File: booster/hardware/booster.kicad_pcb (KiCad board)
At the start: 2 copper layers, 41.1 x 16 mm, 5 parts, among them J1 12V_booster, J4 Conn_01x03, U1 LM2940IMP-10/NOPB

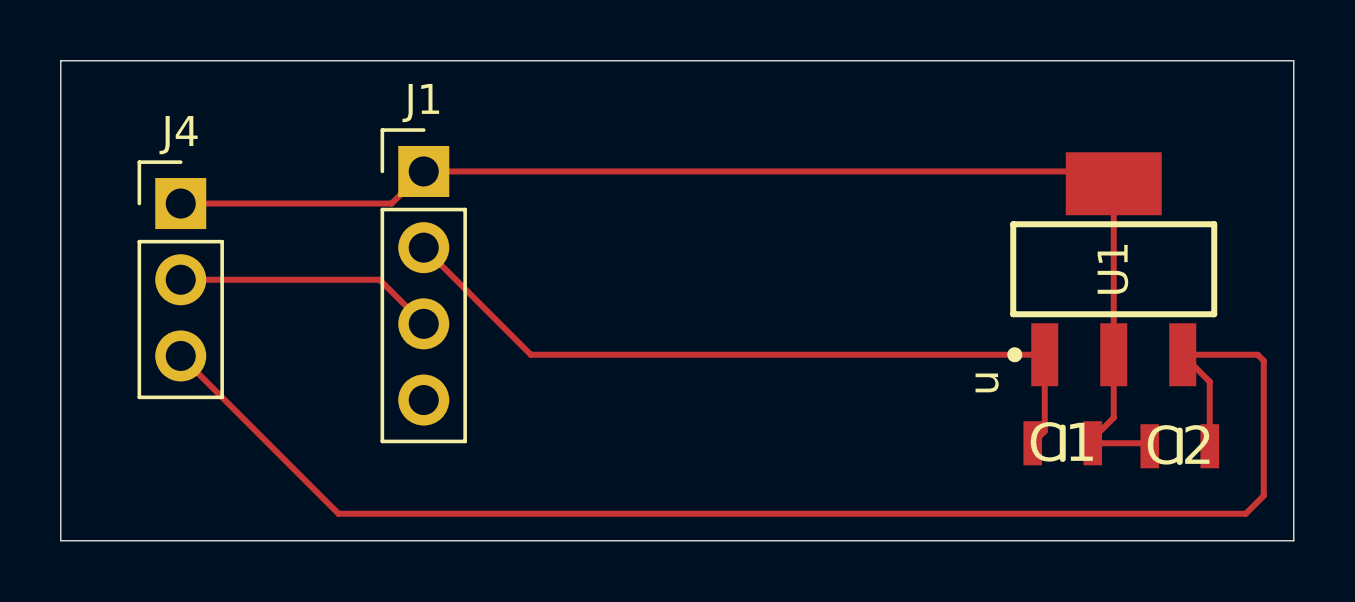
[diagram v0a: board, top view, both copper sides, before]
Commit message: created fab outputs for booster test board
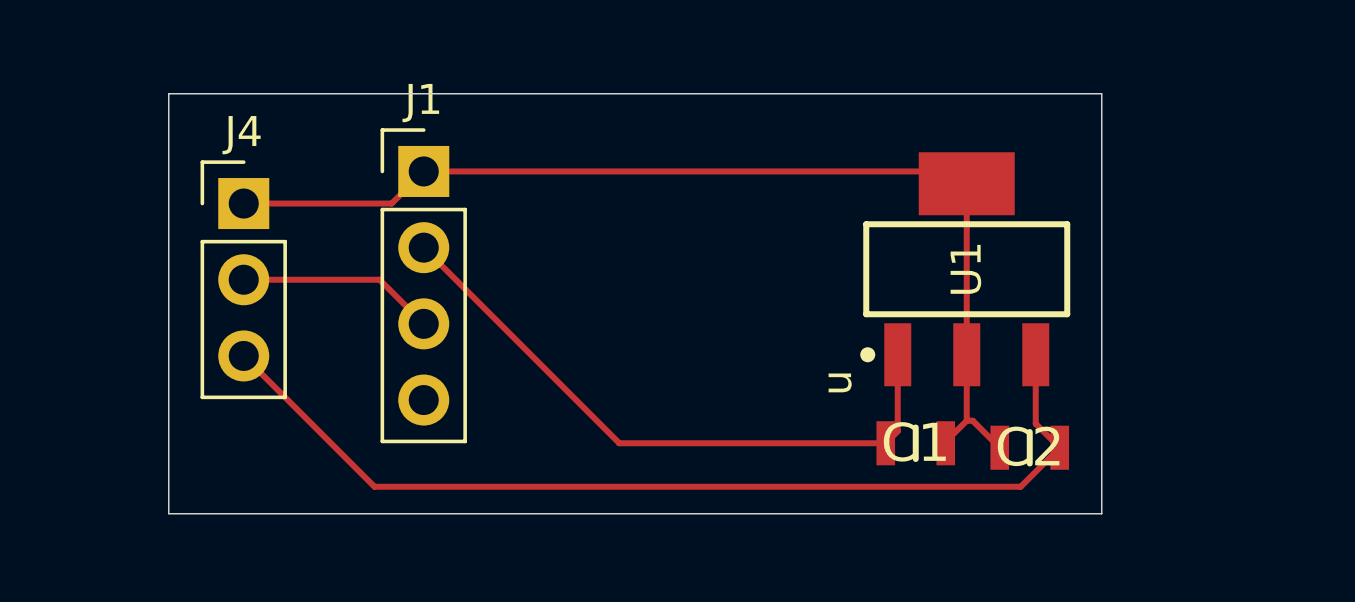
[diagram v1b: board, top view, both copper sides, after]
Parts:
- moved C2 5.00 mm to (147.7, 97.0)
- moved C1 4.90 mm to (143.9, 96.9)
- moved U1 4.90 mm to (145.6, 91.1)
- moved J4 2.10 mm to (121.5, 88.9)
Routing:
- net /10V: track 49.2 -> 33.0 mm
- net GND: track 42.6 -> 35.4 mm
- net /12V: track 25.3 -> 21.2 mm
- net /5V: track 8.71 -> 6.61 mm
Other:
- board size 41.1 x 16 mm -> 31.1 x 14 mm
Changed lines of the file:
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@@
 			(outputformat 1)
 			(mirror no)
-			(drillshape 1)
+			(drillshape 0)
 			(scaleselection 1)
-			(outputdirectory "")
+			(outputdirectory "../outputs/")
 		)
 	)
 	(footprint "Connector_PinHeader_2.54mm:PinHeader_1x03_P2.54mm_Vertical"
 		(layer "F.Cu")
-		(at 119.4 88.86)
+		(at 121.5 88.86)
 		(descr "Through hole straight pin header, 1x03, 2.54mm pitch, single row")
 		(tags "Through hole pin header THT 1x03 2.54mm single row")
@@
 	(footprint "booster:DCY0004A_L"
 		(layer "F.Cu")
-		(at 150.5 91.050001 90)
+		(at 145.6 91.050001 90)
 		(tags "LM2940IMP-10/NOPB ")
 		(property "Reference" "U1"
@@
 	(footprint "booster:CAPC2012X145N"
 		(layer "F.Cu")
-		(at 152.7 96.950001)
+		(at 147.7 97)
 		(descr "C2012 [EIA CC0805]")
 		(tags "Capacitor")
@@
 	(footprint "booster:CAPC2012X145N"
 		(layer "F.Cu")
-		(at 148.8 96.850001 180)
+		(at 143.9 96.850001 180)
 		(descr "C2012 [EIA CC0805]")
 		(tags "Capacitor")
@@
 	)
 	(gr_rect
-		(start 115.4 84.1)
-		(end 156.5 100.1)
+		(start 119 85.2)
+		(end 150.1 99.2)
 		(stroke
 			(width 0.05)
@@
 	)
 	(segment
-		(start 150.089998 87.79)
-		(end 150.5 88.200002)
+		(start 145.6 96.1)
+		(end 145.6 93.9)
 		(width 0.2)
 		(layer "F.Cu")
@@
 	)
 	(segment
-		(start 149.8 96.850001)
-		(end 149.8 96.7)
+		(start 144.9 96.850001)
+		(end 144.9 96.7)
 		(width 0.2)
 		(layer "F.Cu")
@@
 	(segment
 		(start 127.5 87.79)
-		(end 150.089998 87.79)
+		(end 145.189998 87.79)
 		(width 0.2)
 		(layer "F.Cu")
@@
 	)
 	(segment
-		(start 149.8 96.850001)
-		(end 151.6 96.850001)
+		(start 146.7 96.850001)
+		(end 146.8 96.950001)
+		(width 0.2)
+		(layer "F.Cu")
+		(net "GND")
+	)
+	(segment
+		(start 145.189998 87.79)
+		(end 145.6 88.200002)
+		(width 0.2)
+		(layer "F.Cu")
+		(net "GND")
+	)
+	(segment
+		(start 144.9 96.8)
+		(end 145.6 96.1)
+		(width 0.2)
+		(layer "F.Cu")
+		(net "GND")
+	)
+	(segment
+		(start 145.8 96.1)
+		(end 145.6 96.1)
 		(width 0.2)
 		(layer "F.Cu")
@@
 	)
 	(segment
-		(start 151.6 96.850001)
-		(end 151.7 96.950001)
+		(start 146.7 97)
+		(end 145.8 96.1)
 		(width 0.2)
 		(layer "F.Cu")
@@
 	)
 	(segment
-		(start 149.8 96.7)
-		(end 150.5 96)
+		(start 121.5 88.86)
+		(end 126.43 88.86)
 		(width 0.2)
 		(layer "F.Cu")
@@
 	)
 	(segment
-		(start 119.4 88.86)
-		(end 126.43 88.86)
+		(start 144.9 96.850001)
+		(end 144.9 96.8)
 		(width 0.2)
 		(layer "F.Cu")
@@
 	)
 	(segment
-		(start 150.5 88.200002)
-		(end 150.5 93.9)
+		(start 145.6 88.200002)
+		(end 145.6 93.9)
 		(width 0.2)
 		(layer "F.Cu")
 		(net "GND")
-	)
-	(segment
-		(start 150.5 96)
-		(end 150.5 93.9)
-		(width 0.2)
-		(layer "F.Cu")
-		(net "GND")
-	)
-	(segment
-		(start 131.07 93.9)
-		(end 148.2 93.9)
-		(width 0.2)
-		(layer "F.Cu")
-		(net "/12V")
-	)
-	(segment
-		(start 148.2 96.450001)
-		(end 147.8 96.850001)
-		(width 0.2)
-		(layer "F.Cu")
-		(net "/12V")
-	)
-	(segment
-		(start 127.5 90.33)
-		(end 131.07 93.9)
-		(width 0.2)
-		(layer "F.Cu")
-		(net "/12V")
-	)
-	(segment
-		(start 148.2 93.9)
-		(end 148.2 96.450001)
-		(width 0.2)
-		(layer "F.Cu")
-		(net "/12V")
-	)
-	(segment
-		(start 153.7 94.8)
-		(end 152.8 93.9)
-		(width 0.2)
-		(layer "F.Cu")
-		(net "/10V")
-	)
-	(segment
-		(start 155.5 98.6)
-		(end 154.9 99.2)
-		(width 0.2)
-		(layer "F.Cu")
-		(net "/10V")
-	)
-	(segment
-		(start 155.5 94.1)
-		(end 155.5 98.6)
-		(width 0.2)
-		(layer "F.Cu")
-		(net "/10V")
-	)
-	(segment
-		(start 124.66 99.2)
-		(end 119.4 93.94)
-		(width 0.2)
-		(layer "F.Cu")
-		(net "/10V")
-	)
-	(segment
-		(start 154.9 99.2)
-		(end 124.66 99.2)
-		(width 0.2)
-		(layer "F.Cu")
-		(net "/10V")
-	)
-	(segment
-		(start 153.7 96.950001)
-		(end 153.7 94.8)
-		(width 0.2)
-		(layer "F.Cu")
-		(net "/10V")
-	)
-	(segment
-		(start 155.3 93.9)
-		(end 155.5 94.1)
-		(width 0.2)
-		(layer "F.Cu")
-		(net "/10V")
-	)
-	(segment
-		(start 152.8 93.9)
-		(end 155.3 93.9)
-		(width 0.2)
-		(layer "F.Cu")
-		(net "/10V")
-	)
-	(segment
-		(start 126.03 91.4)
-		(end 119.4 91.4)
-		(width 0.2)
-		(layer "F.Cu")
-		(net "/5V")
 	)
 	(segment
@@
 		(net "/5V")
 	)
+	(segment
+		(start 126.03 91.4)
+		(end 121.5 91.4)
+		(width 0.2)
+		(layer "F.Cu")
+		(net "/5V")
+	)
+	(segment
+		(start 148.7 97)
+		(end 147.4 98.3)
+		(width 0.2)
+		(layer "F.Cu")
+		(net "/10V")
+	)
+	(segment
+		(start 125.86 98.3)
+		(end 121.5 93.94)
+		(width 0.2)
+		(layer "F.Cu")
+		(net "/10V")
+	)
+	(segment
+		(start 147.9 96.2)
+		(end 148.7 97)
+		(width 0.2)
+		(layer "F.Cu")
+		(net "/10V")
+	)
+	(segment
+		(start 147.4 98.3)
+		(end 125.86 98.3)
+		(width 0.2)
+		(layer "F.Cu")
+		(net "/10V")
+	)
+	(segment
+		(start 147.9 93.9)
+		(end 147.9 96.2)
+		(width 0.2)
+		(layer "F.Cu")
+		(net "/10V")
+	)
+	(segment
+		(start 143.3 96.450001)
+		(end 142.9 96.850001)
+		(width 0.2)
+		(layer "F.Cu")
+		(net "/12V")
+	)
+	(segment
+		(start 143.3 93.9)
+		(end 143.3 96.450001)
+		(width 0.2)
+		(layer "F.Cu")
+		(net "/12V")
+	)
+	(segment
+		(start 134.020001 96.850001)
+		(end 142.9 96.850001)
+		(width 0.2)
+		(layer "F.Cu")
+		(net "/12V")
+	)
+	(segment
+		(start 127.5 90.33)
+		(end 134.020001 96.850001)
+		(width 0.2)
+		(layer "F.Cu")
+		(net "/12V")
+	)
 	(embedded_fonts no)

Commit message: made booster board pcb
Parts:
- removed J1: 12V_booster, Connector_PinHeader_2.54mm:PinHeader_1x04_P2.54mm_Vertical
- added C3: 10uF, booster:smd_cap_10uf_16V, F.Cu at (134.3, 87.5)
- added C4: 22uF, booster:smd_cap_22uf_16V, F.Cu at (130.3, 92.0)
- added C5: 22pF, booster:CAPC2012X145N, F.Cu at (137.8, 88.0)
- added D1: MBR120VLSFT1G, booster:MBR120VLSFT1G, F.Cu at (137.3, 95.7)
- added L1: MLP2520S100MT0S1, booster:INDC10uh, F.Cu at (130.8, 95.9)
- added R1: 876k, booster:smd_res_876k_KOA, F.Cu at (131.7, 87.9)
- added R2: 100k, booster:smd_res_100k, F.Cu at (129.1, 88.1)
- added R3: 100k, booster:smd_res_100k, F.Cu at (137.0, 91.2)
- added U2: TPS61040DBVR, booster:TPS61040DBVR, F.Cu at (134.2, 92.0)
- moved J4 3.41 mm to (124.9, 88.6)
- moved C1 1.44 mm to (142.7, 96.1)
- moved C2 1.44 mm to (146.5, 96.2)
- moved U1 1.44 mm to (144.4, 90.3)
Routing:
- net Net-(U2-FB): track 0.00 -> 16.6 mm
- net GND: track 35.4 -> 21.8 mm, vias 0 -> 5
- net /5V: track 6.61 -> 19.2 mm
- net Net-(U2-SW): track 0.00 -> 6.50 mm
- net /10V: track 33.0 -> 29.1 mm
- net Net-(U2-EN): track 0.00 -> 1.87 mm
- added copper zone on F.Cu, net GND
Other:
- board size 31.1 x 14 mm -> 28.5 x 13.1 mm

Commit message: made whole pcb
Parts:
- removed J4: Conn_01x03, Connector_PinHeader_2.54mm:PinHeader_1x03_P2.54mm_Vertical
- added J1: i/o, booster:board headers, F.Cu at (121.8, 85.0)
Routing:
- net /10V: track 29.1 -> 28.4 mm
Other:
- board size 28.5 x 13.1 mm -> 30.8 x 13.1 mm

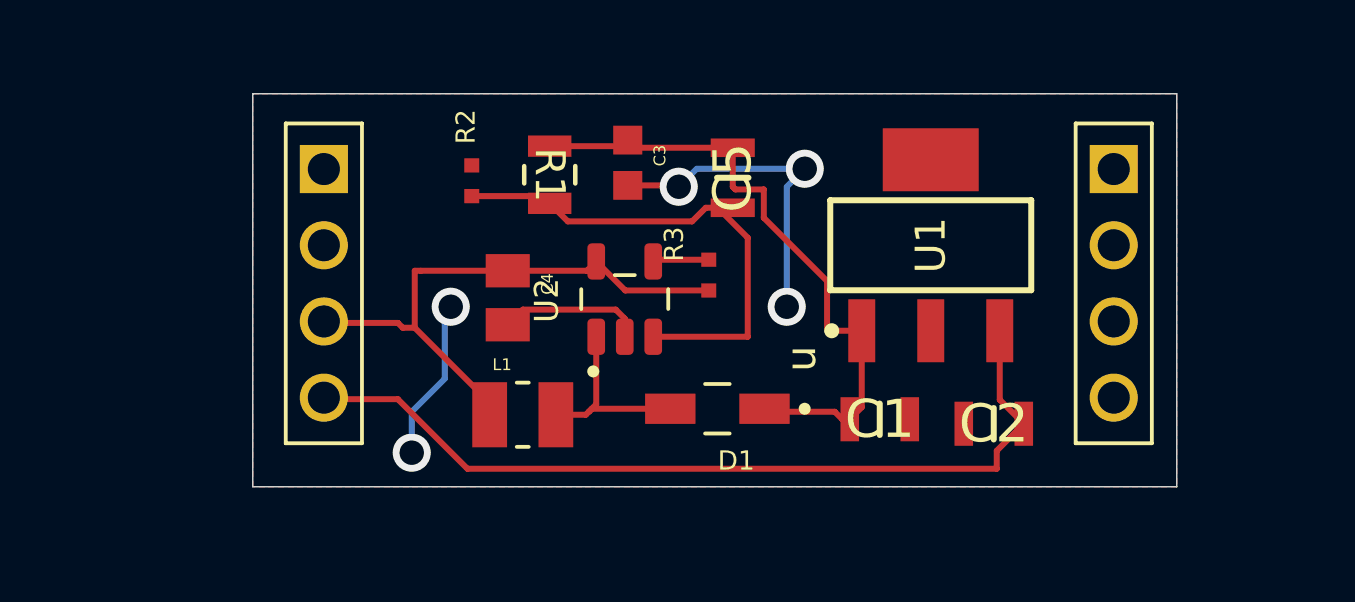
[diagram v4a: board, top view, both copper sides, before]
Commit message: more filtering added to booster
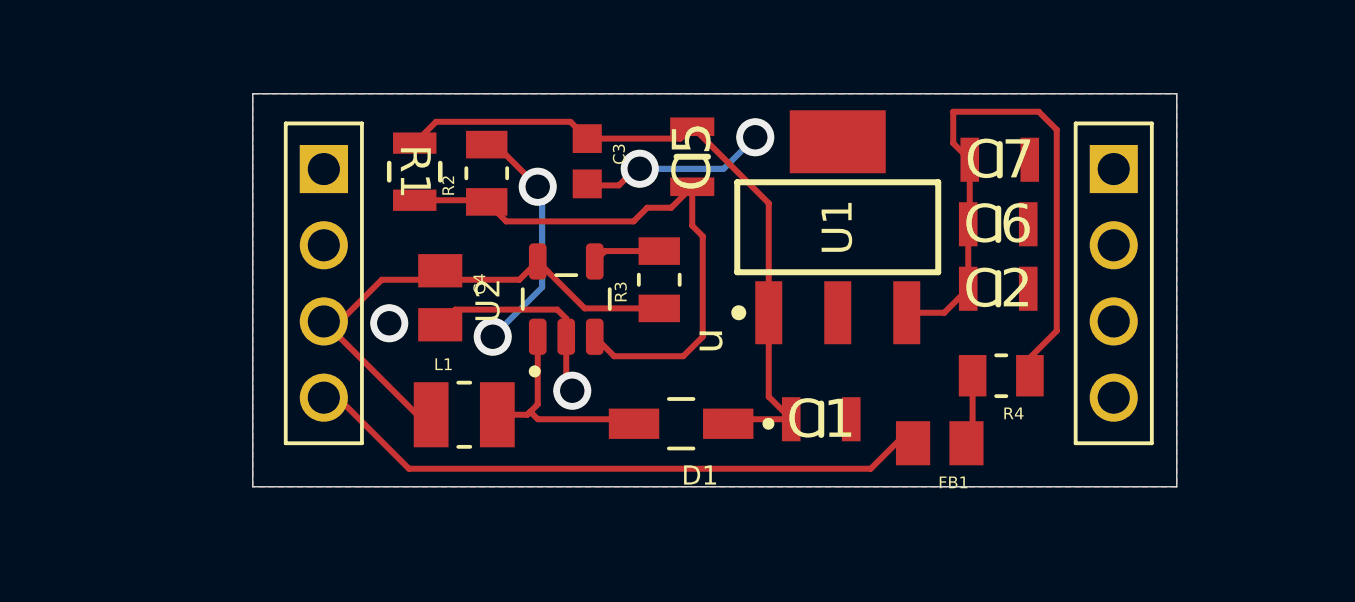
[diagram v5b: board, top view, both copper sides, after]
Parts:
- added C6: 47nF, booster:CAPC2012X145N, F.Cu at (146.7, 89.5)
- added C7: 1uF, booster:CAPC2012X145N, F.Cu at (146.7, 87.4)
- added FB1: FerriteBead, booster:ferrite_220, F.Cu at (144.7, 96.8)
- added R4: 10k, booster:smd_res_10k, F.Cu at (146.8, 94.6)
- R2, R3: footprint booster:smd_res_100k -> booster:smd_res_100k_big
- moved C2 4.50 mm to (146.7, 91.7), turned to 180 degrees
- moved R1 4.50 mm to (127.2, 87.8)
- moved U1 3.16 mm to (141.3, 89.7)
- moved C4 2.25 mm to (128.1, 92.0)
- moved L1 1.95 mm to (128.8, 95.9)
- moved C1 1.95 mm to (140.8, 96.1)
- moved U2 1.95 mm to (132.2, 92.0)
- moved R3 1.66 mm to (135.3, 91.4)
- moved C5 1.52 mm to (136.4, 87.3)
- moved C3 1.35 mm to (132.9, 87.5)
- moved D1 1.31 mm to (136.1, 96.2)
- moved R2 0.56 mm to (129.6, 87.8)
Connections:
- C2 pad 2: /10V -> Net-(U1-OUT)
- J1 pad 8: /10V -> (no net)
- U1 pad 3: /10V -> Net-(U1-OUT)
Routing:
- net Net-(U1-OUT): track 0.00 -> 20.9 mm
- net /10V: track 28.4 -> 21.4 mm
- net /12V: track 21.1 -> 24.2 mm
- net Net-(U2-FB): track 16.6 -> 19.3 mm
- net Net-(FB1-Pad1): track 0.00 -> 1.50 mm
- net /5V: track 18.9 -> 17.9 mm
- net Net-(U2-SW): track 6.50 -> 7.37 mm
- net GND: track 21.6 -> 22.0 mm, vias 5 -> 6
- added copper zone on B.Cu, net GND
